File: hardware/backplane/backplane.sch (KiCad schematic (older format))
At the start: 107 parts, among them J1 C96ABC, J10 Conn_Coaxial_Power, J2 C96ABC, J3 C96ABC, J4 C96ABC, J5 C96ABC, J6 C96ABC, J7 C96ABC, J8 C96ABC, J9 C96ABC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

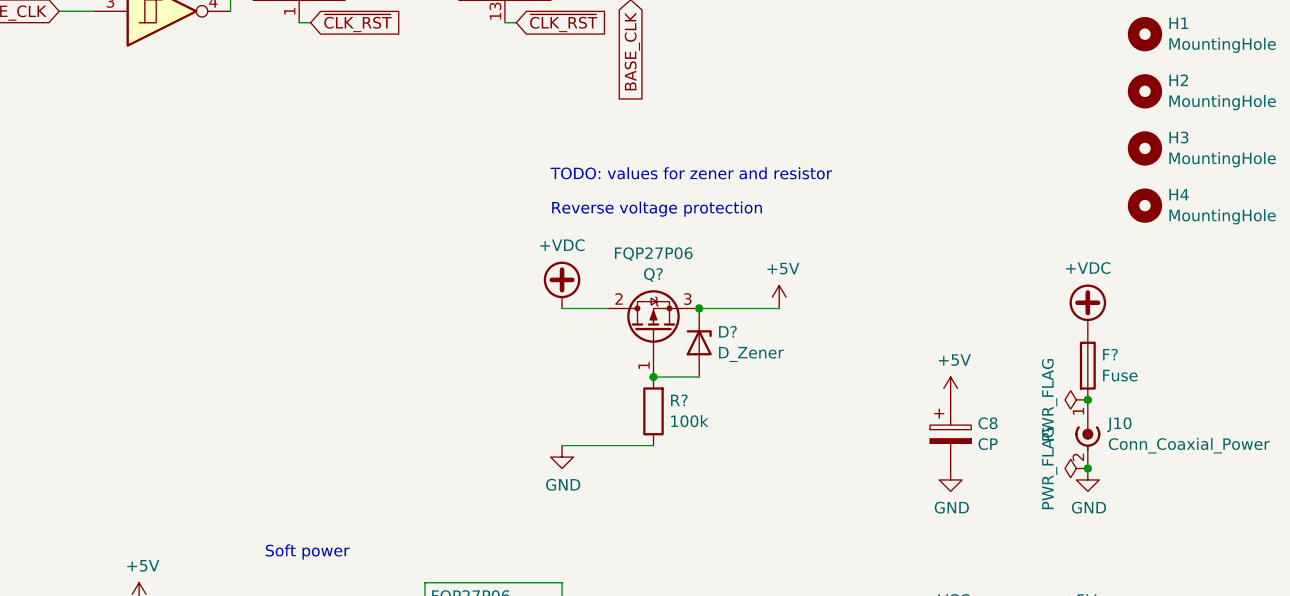
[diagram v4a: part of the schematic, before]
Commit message: backplane: fix some values and footprints
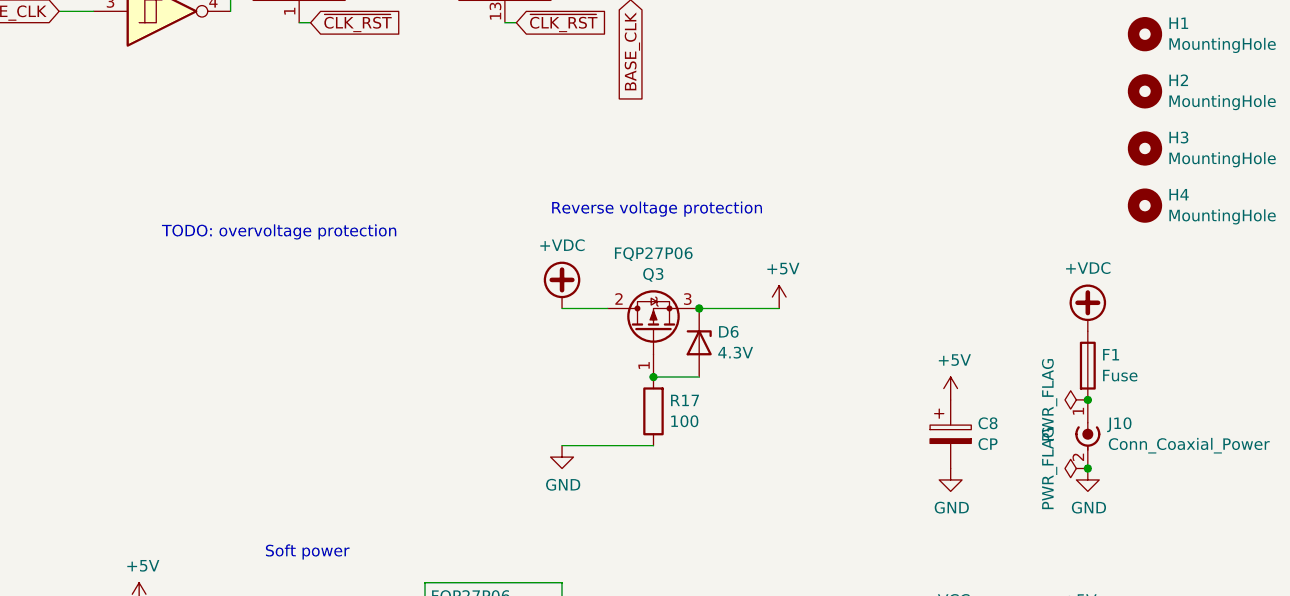
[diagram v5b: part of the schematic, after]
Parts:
- D6: renamed from D?; value D_Zener -> 4.3V
- F1: renamed from F?; footprint (none) -> Fuse:Fuse_BelFuse_0ZRE0125FF_L21.2mm_W5.3mm
- R17: renamed from R?; value 100k -> 100
- gave numbers to parts that had none: 1
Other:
- note added: "TODO: overvoltage protection"
- note removed: "TODO: values for zener and resistor"
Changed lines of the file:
@@
 	8000 4000 7800 4000
 $Comp
-L Device:R R?
+L Device:R R17
 U 1 1 67F57805
 P 8200 4450
-F 0 "R?" H 8130 4404 50  0000 R CNN
-F 1 "100k" H 8130 4495 50  0000 R CNN
+F 0 "R17" H 8130 4404 50  0000 R CNN
+F 1 "100" H 8130 4495 50  0000 R CNN
 F 2 "Resistor_THT:R_Axial_DIN0207_L6.3mm_D2.5mm_P7.62mm_Horizontal" V 8130 4450 50  0001 C CNN
 F 3 "~" H 8200 4450 50  0001 C CNN
@@
 Connection ~ 8200 4300
 $Comp
-L Transistor_FET:FQP27P06 Q?
+L Transistor_FET:FQP27P06 Q3
 U 1 1 6743CEED
 P 8200 4100
-F 0 "Q?" V 8449 4100 50  0000 C CNN
+F 0 "Q3" V 8449 4100 50  0000 C CNN
 F 1 "FQP27P06" V 8540 4100 50  0000 C CNN
 F 2 "Package_TO_SOT_THT:TO-220-3_Horizontal_TabDown" H 8400 4025 50  0001 L CIN
@@
 $EndComp
 $Comp
-L Device:D_Zener D?
+L Device:D_Zener D6
 U 1 1 68F47E00
 P 8400 4150
-F 0 "D?" V 8354 4230 50  0000 L CNN
-F 1 "D_Zener" V 8445 4230 50  0000 L CNN
+F 0 "D6" V 8354 4230 50  0000 L CNN
+F 1 "4.3V" V 8445 4230 50  0000 L CNN
 F 2 "Diode_THT:D_A-405_P7.62mm_Horizontal" H 8400 4150 50  0001 C CNN
 F 3 "~" H 8400 4150 50  0001 C CNN
@@
 Connection ~ 10100 4400
 $Comp
-L Device:Fuse F?
+L Device:Fuse F1
 U 1 1 68F4D08F
 P 10100 4250
-F 0 "F?" H 10160 4296 50  0000 L CNN
+F 0 "F1" H 10160 4296 50  0000 L CNN
 F 1 "Fuse" H 10160 4205 50  0000 L CNN
-F 2 "" V 10030 4250 50  0001 C CNN
+F 2 "Fuse:Fuse_BelFuse_0ZRE0125FF_L21.2mm_W5.3mm" V 10030 4250 50  0001 C CNN
 F 3 "~" H 10100 4250 50  0001 C CNN
 	1    10100 4250
@@
 Text Notes 7750 3600 0    50   ~ 0
 Reverse voltage protection
-Text Notes 7750 3450 0    50   ~ 0
-TODO: values for zener and resistor
+Text Notes 6050 3700 0    50   ~ 0
+TODO: overvoltage protection
 $EndSCHEMATC

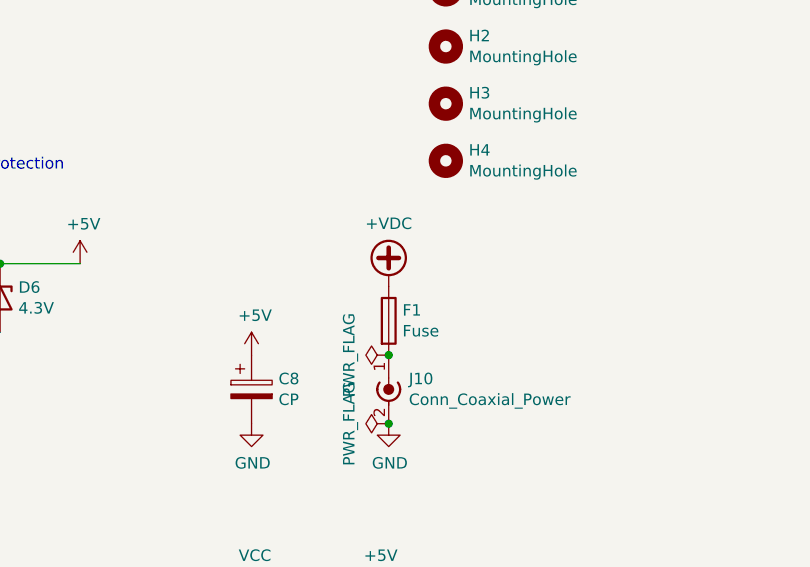
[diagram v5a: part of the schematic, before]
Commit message: backplane: remove fuse
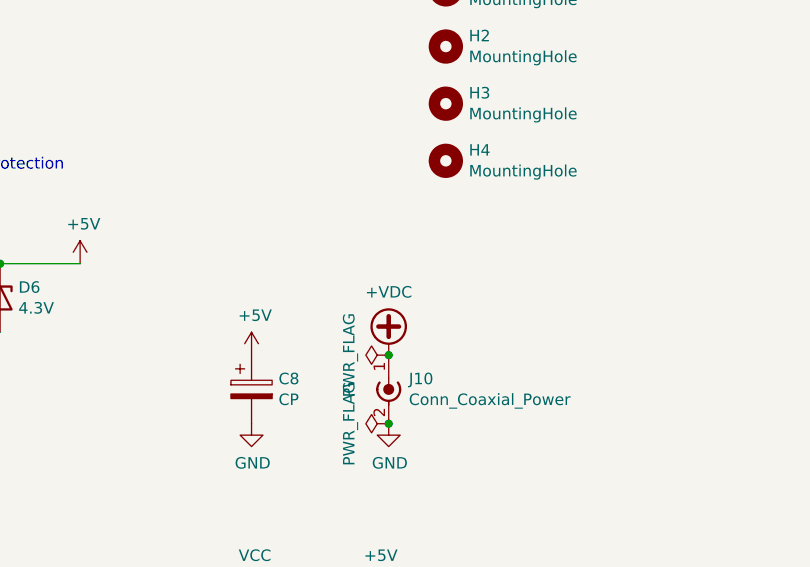
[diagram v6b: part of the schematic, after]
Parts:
- removed F1: Fuse, Fuse:Fuse_BelFuse_0ZRE0125FF_L21.2mm_W5.3mm, symbol Device:Fuse
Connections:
- net +VDC: now also J10.1 (In)
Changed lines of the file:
@@
 L power:+VDC #PWR0110
 U 1 1 6776F79E
-P 10100 4100
-F 0 "#PWR0110" H 10100 4000 50  0001 C CNN
-F 1 "+VDC" H 10100 4375 50  0000 C CNN
-F 2 "" H 10100 4100 50  0001 C CNN
-F 3 "" H 10100 4100 50  0001 C CNN
-	1    10100 4100
+P 10100 4400
+F 0 "#PWR0110" H 10100 4300 50  0001 C CNN
+F 1 "+VDC" H 10100 4675 50  0000 C CNN
+F 2 "" H 10100 4400 50  0001 C CNN
+F 3 "" H 10100 4400 50  0001 C CNN
+	1    10100 4400
 	1    0    0    -1
 $EndComp
@@
 $EndComp
 Connection ~ 8400 4000
-Connection ~ 10100 4400
-$Comp
-L Device:Fuse F1
-U 1 1 68F4D08F
-P 10100 4250
-F 0 "F1" H 10160 4296 50  0000 L CNN
-F 1 "Fuse" H 10160 4205 50  0000 L CNN
-F 2 "Fuse:Fuse_BelFuse_0ZRE0125FF_L21.2mm_W5.3mm" V 10030 4250 50  0001 C CNN
-F 3 "~" H 10100 4250 50  0001 C CNN
-	1    10100 4250
-	1    0    0    -1
-$EndComp
 Text Notes 6500 5100 0    50   ~ 0
 Soft power
@@
 Text Notes 6050 3700 0    50   ~ 0
 TODO: overvoltage protection
+Connection ~ 10100 4400
 $EndSCHEMATC

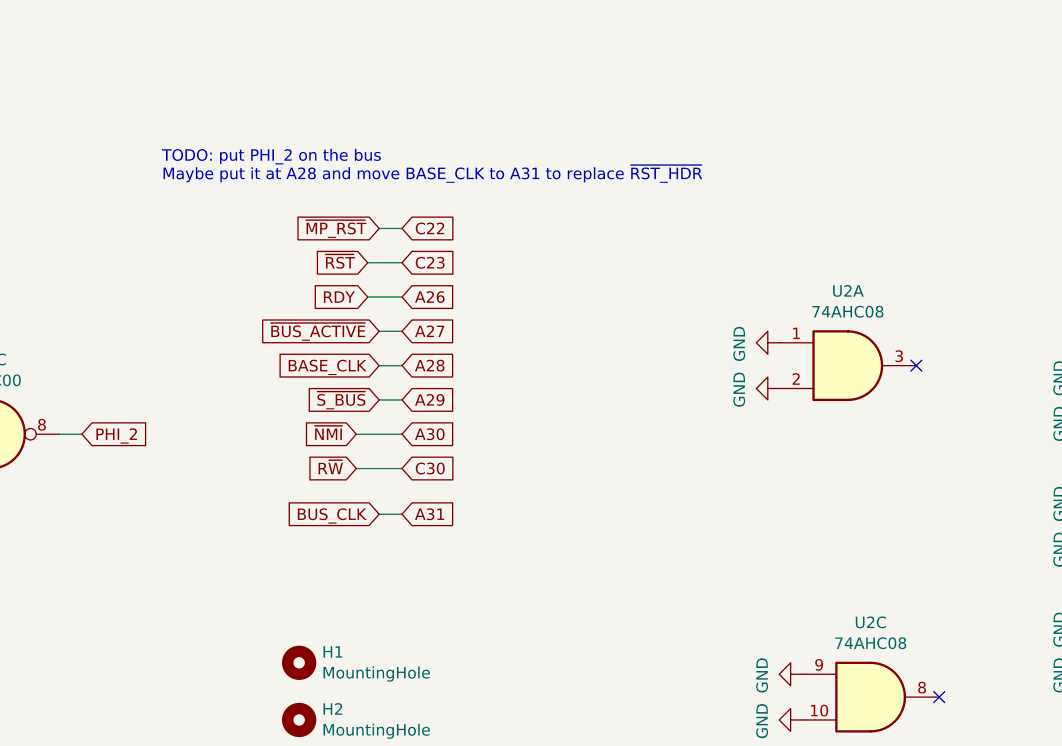
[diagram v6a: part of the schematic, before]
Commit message: document existing bus signals properly in backplane
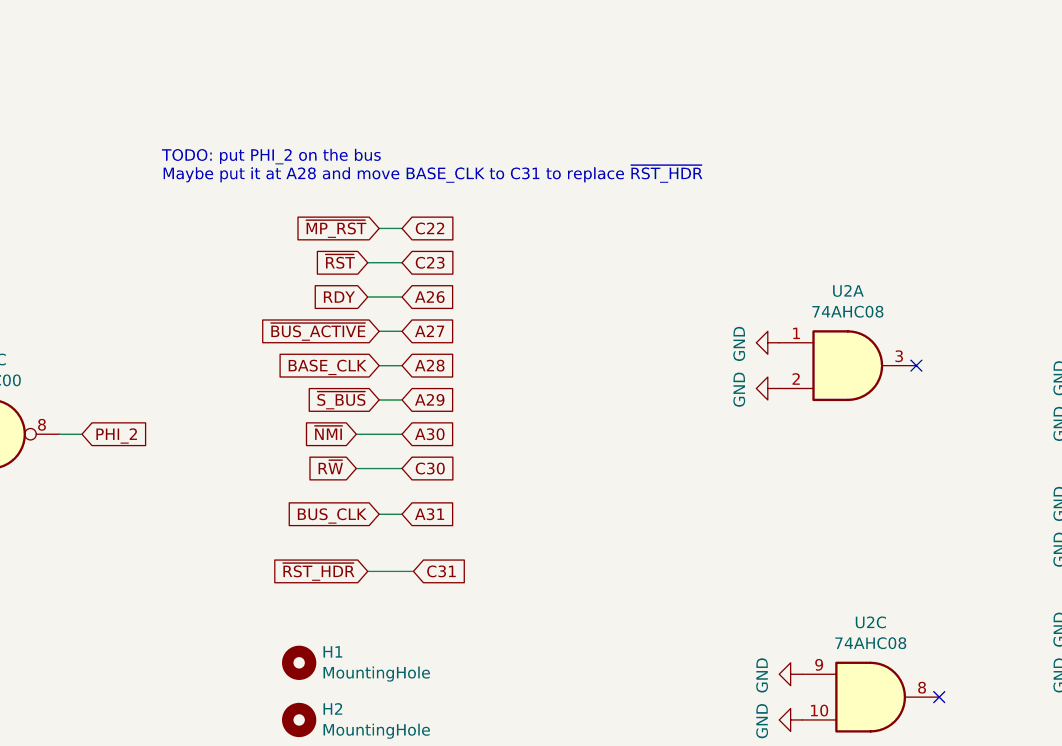
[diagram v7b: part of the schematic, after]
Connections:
- net ~RST_HDR~ is gone; now on net C31: D3.1 (K), D5.1 (K), R1.2, SW4.2
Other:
- note added: "TODO: put PHI_2 on the bus\nMaybe put it at A28 and move BASE_CLK to C31 to replace ~RST_HDR~"
- note removed: "TODO: put PHI_2 on the bus\nMaybe put it at A28 and move BASE_CLK to A31 to replace ~RST_HDR~"
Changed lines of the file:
@@
 NoConn ~ 14450 2750
 Text Notes 9750 700  0    50   ~ 0
-TODO: put PHI_2 on the bus\nMaybe put it at A28 and move BASE_CLK to A31 to replace ~RST_HDR~
+TODO: put PHI_2 on the bus\nMaybe put it at A28 and move BASE_CLK to C31 to replace ~RST_HDR~
 $Comp
 L Device:C CBX1
@@
 TODO: overvoltage protection
 Connection ~ 10100 4400
+Text GLabel 10650 2400 0    50   Input ~ 0
+~RST_HDR~
+Text GLabel 10850 2400 2    50   Input ~ 0
+C31
+Wire Wire Line
+	10850 2400 10650 2400
 $EndSCHEMATC

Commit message: more backplane comments
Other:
- note added: "BASE_CLK is the clock signal generated by the crystal oscillator or the 555\nPHI_2 is the effective clock signal, which may be controlled by a bus device if ~BUS_ACTIVE~ is low"
- note added: "TODO: overvoltage protection\n(not doing this for now)"
- note added: "TODO: put PHI_2 on the bus - bus devices could use this to ensure\nthat they have a consistent view on what the effective clock speed \nof the system is\nMaybe put it at A28 and move BASE_CLK to C31 to replace ~RST_HDR~\n~RST_HDR~ is unnecessary as the reset signal is handled by a header on the backplane"
- note removed: "TODO: overvoltage protection"
- note removed: "TODO: put PHI_2 on the bus\nMaybe put it at A28 and move BASE_CLK to C31 to replace ~RST_HDR~"
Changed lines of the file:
@@
 NoConn ~ 14450 2200
 NoConn ~ 14450 2750
-Text Notes 9750 700  0    50   ~ 0
-TODO: put PHI_2 on the bus\nMaybe put it at A28 and move BASE_CLK to C31 to replace ~RST_HDR~
+Text Notes 9600 550  0    50   ~ 0
+TODO: put PHI_2 on the bus - bus devices could use this to ensure\nthat they have a consistent view on what the effective clock speed \nof the system is\nMaybe put it at A28 and move BASE_CLK to C31 to replace ~RST_HDR~\n~RST_HDR~ is unnecessary as the reset signal is handled by a header on the backplane
 $Comp
 L Device:C CBX1
@@
 Text Notes 7750 3600 0    50   ~ 0
 Reverse voltage protection
-Text Notes 6050 3700 0    50   ~ 0
-TODO: overvoltage protection
+Text Notes 6000 3750 0    50   ~ 0
+TODO: overvoltage protection\n(not doing this for now)
 Connection ~ 10100 4400
 Text GLabel 10650 2400 0    50   Input ~ 0
@@
 Wire Wire Line
 	10850 2400 10650 2400
+Text Notes 9600 100  0    50   ~ 0
+BASE_CLK is the clock signal generated by the crystal oscillator or the 555\nPHI_2 is the effective clock signal, which may be controlled by a bus device if ~BUS_ACTIVE~ is low
 $EndSCHEMATC
